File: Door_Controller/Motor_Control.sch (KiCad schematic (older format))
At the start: 7 parts

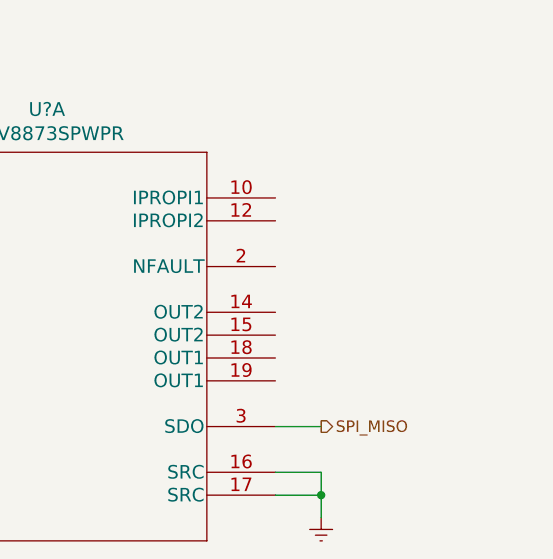
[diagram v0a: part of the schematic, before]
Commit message: wire window motor supply and output
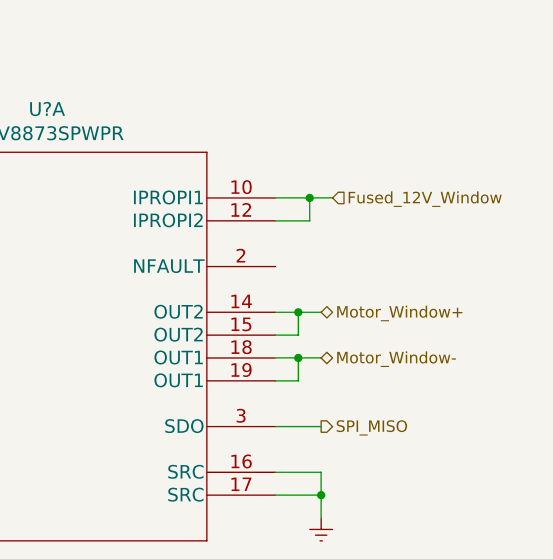
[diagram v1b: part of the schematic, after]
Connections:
- net Fused_12V_Window: now reaches U?.10 (IPROPI1)
- net Fused_12V_Window: now also U?.12 (IPROPI2)
- net Motor_Window+: now reaches U?.14 (OUT2)
- net Motor_Window+: now also U?.15 (OUT2)
- net Motor_Window-: now reaches U?.18 (OUT1)
- net Motor_Window-: now also U?.19 (OUT1)
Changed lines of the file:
@@
 Wire Wire Line
 	2350 4750 2800 4750
+Text HLabel 5050 4550 2    50   Input ~ 0
+Fused_12V_Window
+Wire Wire Line
+	5050 4550 4950 4550
+Wire Wire Line
+	4800 4650 4950 4650
+Wire Wire Line
+	4950 4650 4950 4550
+Connection ~ 4950 4550
+Wire Wire Line
+	4950 4550 4800 4550
+Text HLabel 5000 5050 2    50   BiDi ~ 0
+Motor_Window+
+Text HLabel 5000 5250 2    50   BiDi ~ 0
+Motor_Window-
+Wire Wire Line
+	5000 5050 4900 5050
+Wire Wire Line
+	5000 5250 4900 5250
+Wire Wire Line
+	4800 5350 4900 5350
+Wire Wire Line
+	4900 5350 4900 5250
+Connection ~ 4900 5250
+Wire Wire Line
+	4900 5250 4800 5250
+Wire Wire Line
+	4800 5150 4900 5150
+Wire Wire Line
+	4900 5150 4900 5050
+Connection ~ 4900 5050
+Wire Wire Line
+	4900 5050 4800 5050
 $EndSCHEMATC

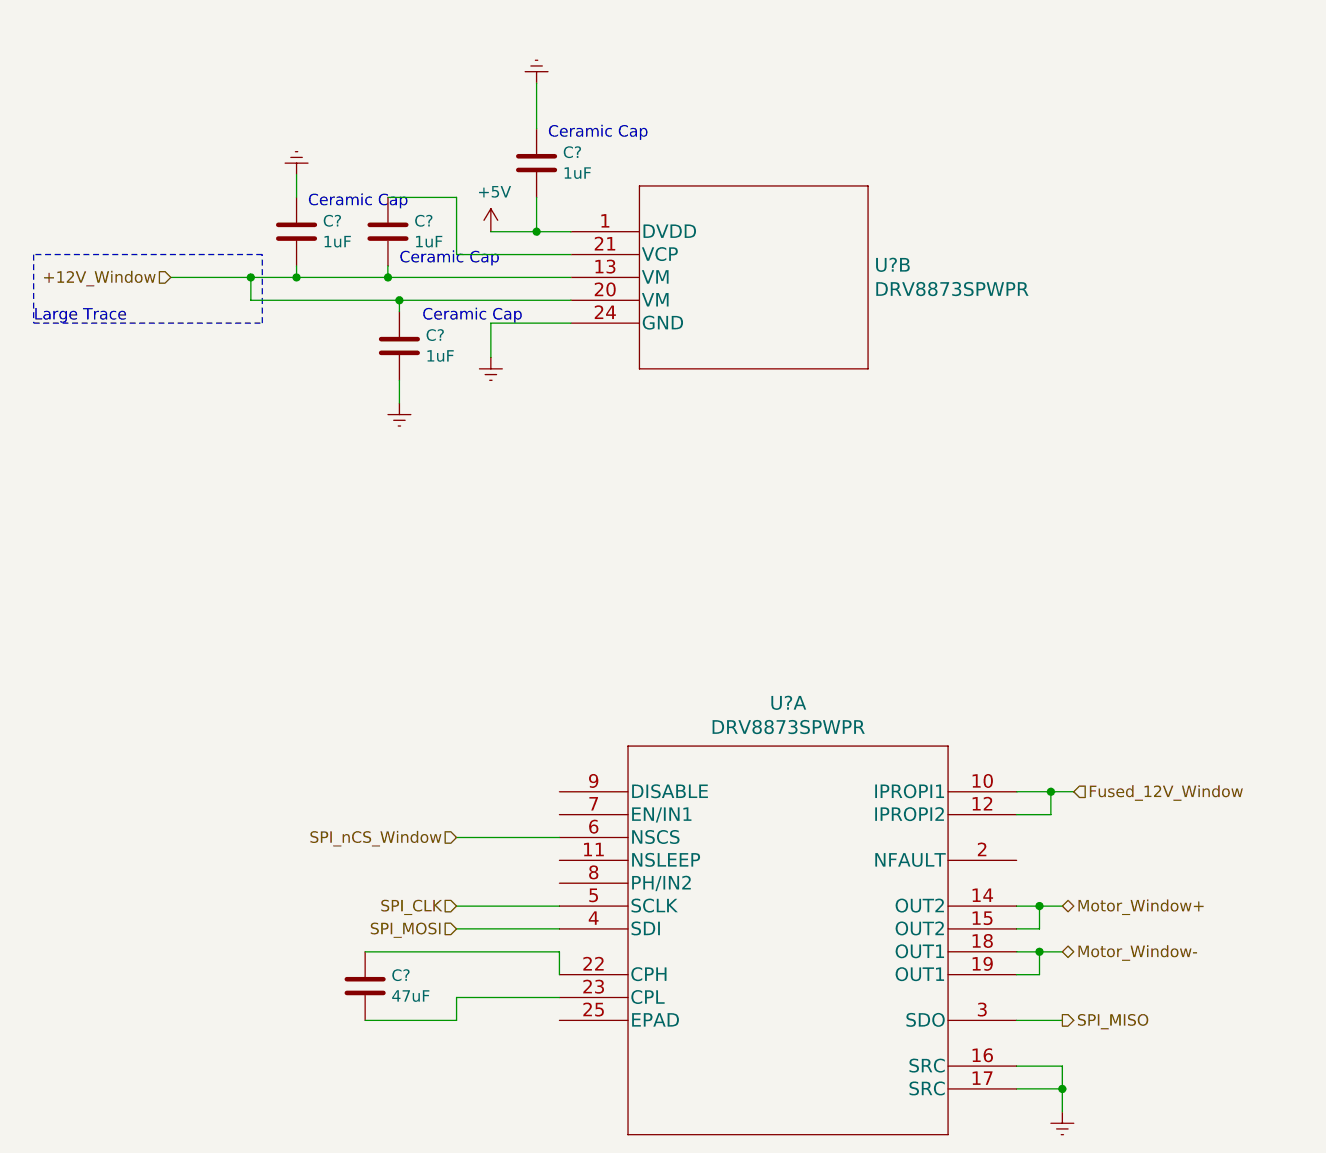
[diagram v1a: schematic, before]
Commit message: add window motor current sense
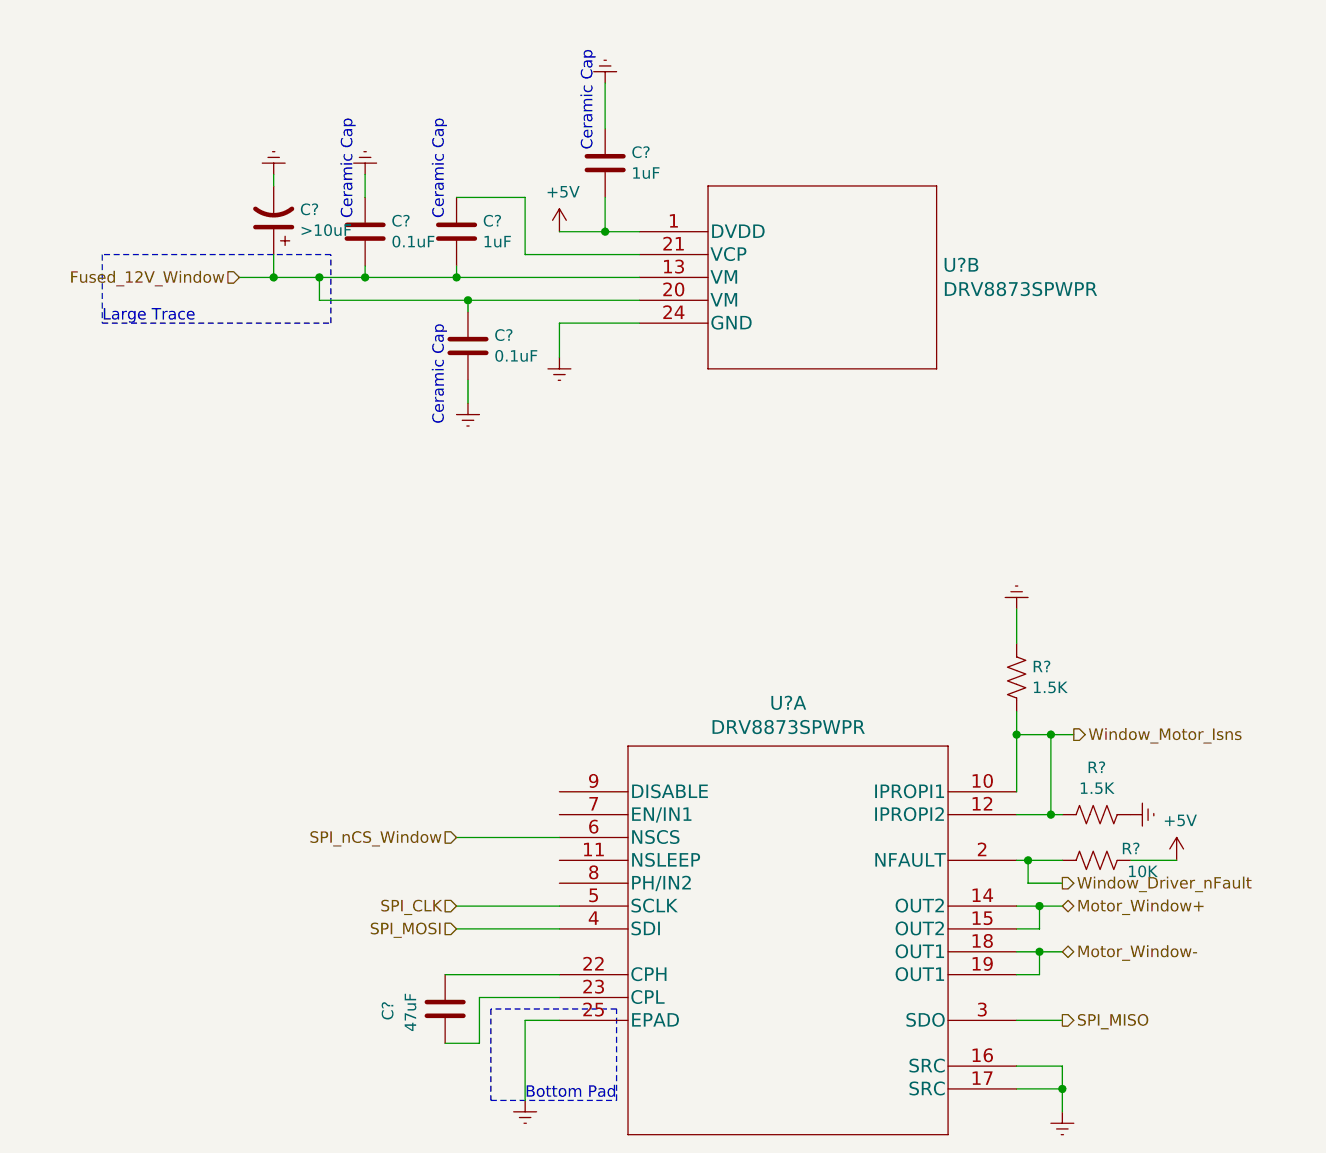
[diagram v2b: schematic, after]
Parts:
- added C?: >10uF, symbol Device:CP1
- added R? (x2): 1.5K, symbol Device:R_US
- added R?: 10K, symbol Device:R_US
- C? (x2): value 1uF -> 0.1uF
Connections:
- net +12V_Window is gone; now on net Fused_12V_Window: C?.1, C?.2, C?.2, U?.13 (VM), U?.20 (VM)
- net +5V: now also R?.2
- net Earth: now also U?.25 (EPAD), C?.2, R?.1, R?.1
- net Fused_12V_Window: now also C?.1; no longer U?.10 (IPROPI1), U?.12 (IPROPI2)
- net Window_Driver_nFault: now reaches U?.2 (NFAULT)
- net Window_Driver_nFault: now also R?.1
- new net Window_Motor_Isns: R?.2, R?.2, U?.10 (IPROPI1), U?.12 (IPROPI2)
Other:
- note added: "Bottom Pad"
- moved on the sheet: C?, U?B

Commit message: "finish" window motor controller
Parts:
- added C? (x2): 1uF, symbol Device:C
- added R? (x2): 1.5K, symbol Device:R_US
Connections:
- net +5V: now also U?.11 (NSLEEP), C?.1
- net Earth: now also C?.1, C?.2, R?.2, R?.2
- net at U?.7 (EN/IN1): now also R?.1
- net at U?.8 (PH/IN2): now also R?.1
- net Window_Ctrl_nDisable: now reaches U?.9 (DISABLE)
- net Window_Ctrl_nDisable: now also C?.2
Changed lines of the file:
@@
 	0    1    1    0
 $EndComp
+$Comp
+L power:Earth #PWR?
+U 1 1 5FBE9744
+P 2300 4650
+F 0 "#PWR?" H 2300 4400 50  0001 C CNN
+F 1 "Earth" H 2300 4500 50  0001 C CNN
+F 2 "" H 2300 4650 50  0001 C CNN
+F 3 "~" H 2300 4650 50  0001 C CNN
+	1    2300 4650
+	0    1    1    0
+$EndComp
+$Comp
+L power:Earth #PWR?
+U 1 1 5FBEA1C6
+P 2300 4950
+F 0 "#PWR?" H 2300 4700 50  0001 C CNN
+F 1 "Earth" H 2300 4800 50  0001 C CNN
+F 2 "" H 2300 4950 50  0001 C CNN
+F 3 "~" H 2300 4950 50  0001 C CNN
+	1    2300 4950
+	0    1    1    0
+$EndComp
+$Comp
+L Device:R_US R?
+U 1 1 5FBEA830
+P 2550 4950
+F 0 "R?" V 2600 5100 50  0000 C CNN
+F 1 "1.5K" V 2500 5100 50  0000 C CNN
+F 2 "" V 2590 4940 50  0001 C CNN
+F 3 "~" H 2550 4950 50  0001 C CNN
+	1    2550 4950
+	0    1    1    0
+$EndComp
+Wire Wire Line
+	2700 4950 2800 4950
+Wire Wire Line
+	2400 4950 2300 4950
+$Comp
+L Device:R_US R?
+U 1 1 5FBED892
+P 2550 4650
+F 0 "R?" V 2600 4800 50  0000 C CNN
+F 1 "1.5K" V 2500 4800 50  0000 C CNN
+F 2 "" V 2590 4640 50  0001 C CNN
+F 3 "~" H 2550 4650 50  0001 C CNN
+	1    2550 4650
+	0    1    1    0
+$EndComp
+Wire Wire Line
+	2300 4650 2400 4650
+Wire Wire Line
+	2700 4650 2800 4650
+$Comp
+L power:Earth #PWR?
+U 1 1 5FBF1639
+P 1400 5400
+F 0 "#PWR?" H 1400 5150 50  0001 C CNN
+F 1 "Earth" H 1400 5250 50  0001 C CNN
+F 2 "" H 1400 5400 50  0001 C CNN
+F 3 "~" H 1400 5400 50  0001 C CNN
+	1    1400 5400
+	1    0    0    -1
+$EndComp
+$Comp
+L Device:C C?
+U 1 1 5FBF1C79
+P 1400 5150
+F 0 "C?" H 1515 5196 50  0000 L CNN
+F 1 "1uF" H 1515 5105 50  0000 L CNN
+F 2 "" H 1438 5000 50  0001 C CNN
+F 3 "~" H 1400 5150 50  0001 C CNN
+	1    1400 5150
+	1    0    0    -1
+$EndComp
+$Comp
+L power:+5V #PWR?
+U 1 1 5FBF2E2E
+P 1400 4800
+F 0 "#PWR?" H 1400 4650 50  0001 C CNN
+F 1 "+5V" H 1415 4973 50  0000 C CNN
+F 2 "" H 1400 4800 50  0001 C CNN
+F 3 "" H 1400 4800 50  0001 C CNN
+	1    1400 4800
+	1    0    0    -1
+$EndComp
+Wire Wire Line
+	1400 5400 1400 5300
+Wire Wire Line
+	1400 5000 1400 4850
+Wire Wire Line
+	2800 4850 1400 4850
+Connection ~ 1400 4850
+Wire Wire Line
+	1400 4850 1400 4800
+Text HLabel 2350 4550 0    50   Input ~ 0
+Window_Ctrl_nDisable
+$Comp
+L Device:C C?
+U 1 1 5FBF9A3D
+P 2500 4300
+F 0 "C?" H 2615 4346 50  0000 L CNN
+F 1 "1uF" H 2615 4255 50  0000 L CNN
+F 2 "" H 2538 4150 50  0001 C CNN
+F 3 "~" H 2500 4300 50  0001 C CNN
+	1    2500 4300
+	1    0    0    -1
+$EndComp
+$Comp
+L power:Earth #PWR?
+U 1 1 5FBFA2FE
+P 2500 4050
+F 0 "#PWR?" H 2500 3800 50  0001 C CNN
+F 1 "Earth" H 2500 3900 50  0001 C CNN
+F 2 "" H 2500 4050 50  0001 C CNN
+F 3 "~" H 2500 4050 50  0001 C CNN
+	1    2500 4050
+	-1   0    0    1
+$EndComp
+Wire Wire Line
+	2500 4050 2500 4150
+Wire Wire Line
+	2350 4550 2500 4550
+Wire Wire Line
+	2500 4450 2500 4550
+Connection ~ 2500 4550
+Wire Wire Line
+	2500 4550 2800 4550
 $EndSCHEMATC
